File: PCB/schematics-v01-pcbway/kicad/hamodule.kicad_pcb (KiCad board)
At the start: 2 copper layers, 78.4 x 84.3 mm, 10 parts, among them J1 Conn_01x05_Female, J2 Conn_01x05_Female

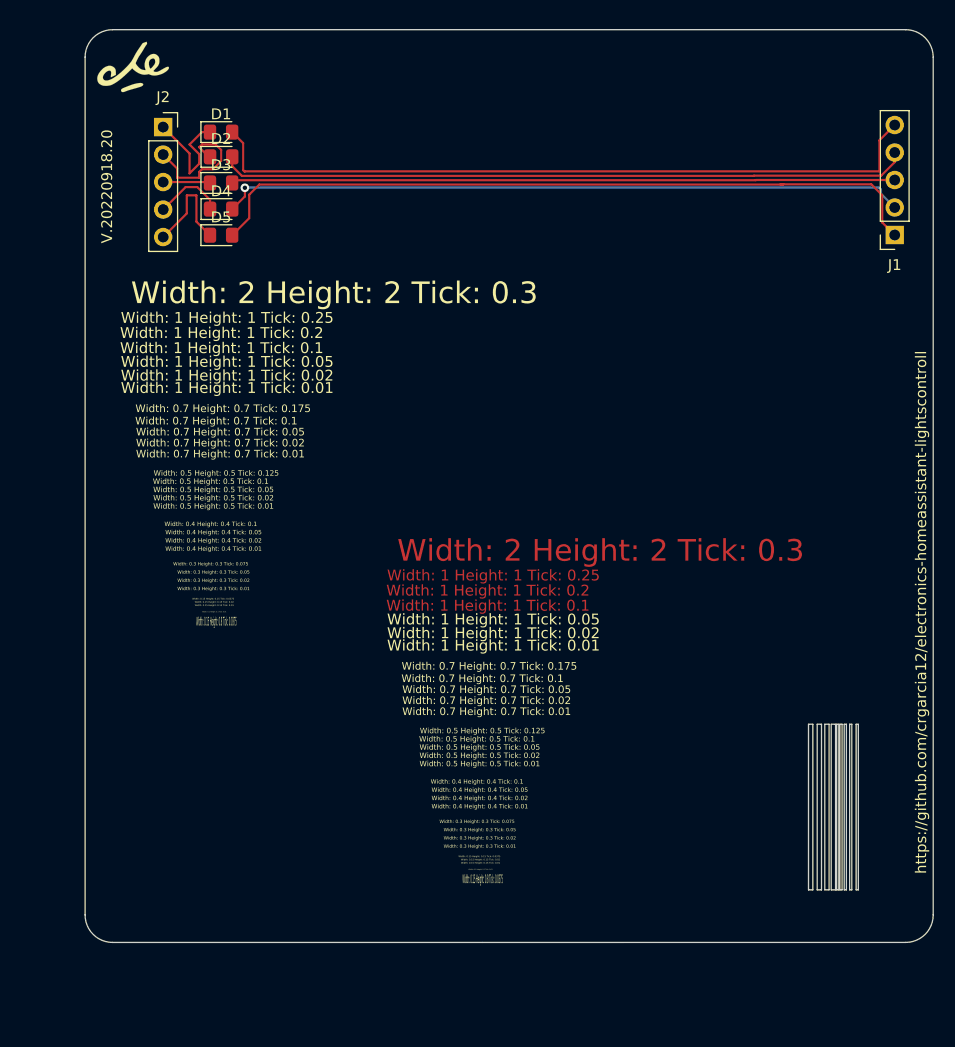
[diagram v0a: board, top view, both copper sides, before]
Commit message: typo in silkscreen
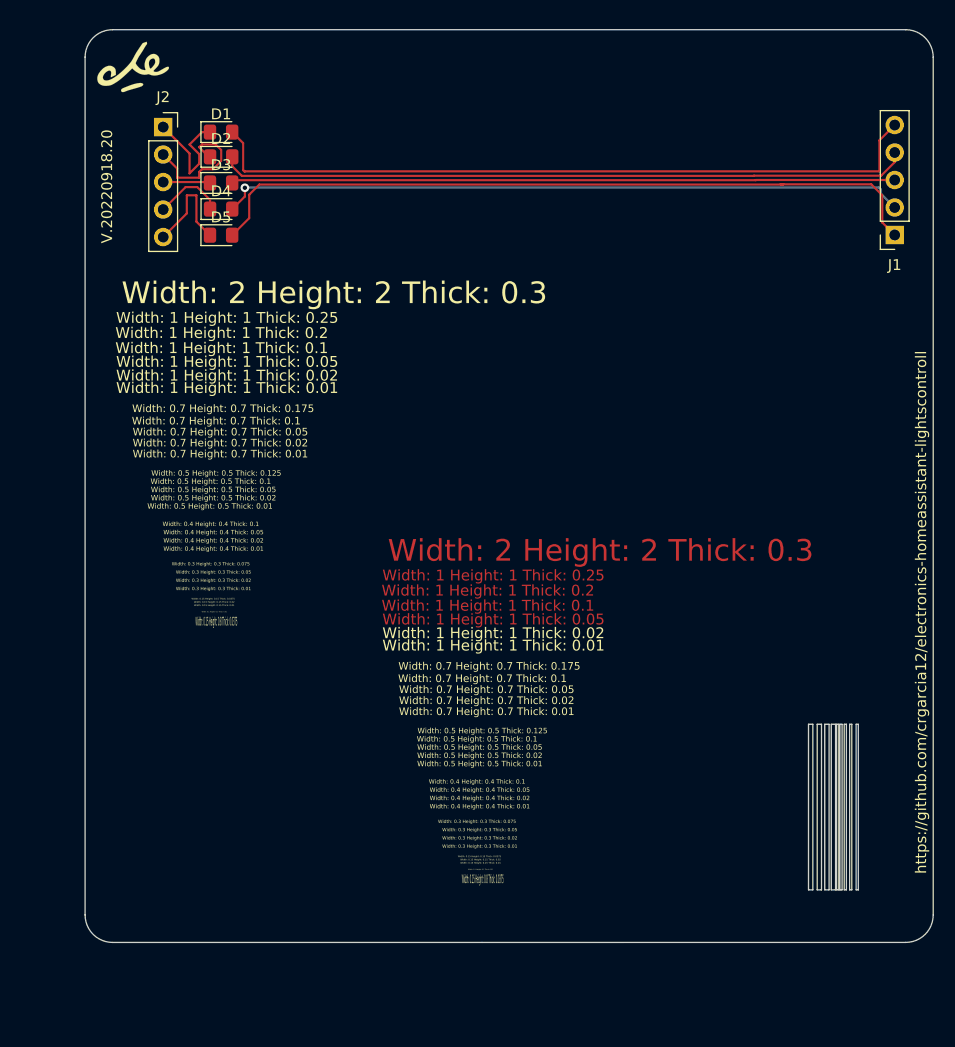
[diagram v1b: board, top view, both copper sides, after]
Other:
- board text added: "Width: 0.1 Height: 0.1 Thick: 0.01"
- board text added: "Width: 0.15 Height: 0.15 Thick: 0.01"
- board text added: "Width: 0.15 Height: 0.15 Thick: 0.02"
- board text added: "Width: 0.15 Height: 0.15 Thick: 0.0375"
- board text added: "Width: 0.15 Height: 0.8 Thick: 0.0375"
- board text added: "Width: 0.3 Height: 0.3 Thick: 0.01"
- board text added: "Width: 0.3 Height: 0.3 Thick: 0.02"
- board text added: "Width: 0.3 Height: 0.3 Thick: 0.05"
- board text added: "Width: 0.3 Height: 0.3 Thick: 0.075"
- board text added: "Width: 0.4 Height: 0.4 Thick: 0.01"
- board text added: "Width: 0.4 Height: 0.4 Thick: 0.02"
- board text added: "Width: 0.4 Height: 0.4 Thick: 0.05"
- board text added: "Width: 0.4 Height: 0.4 Thick: 0.1"
- board text added: "Width: 0.5 Height: 0.5 Thick: 0.01"
- board text added: "Width: 0.5 Height: 0.5 Thick: 0.02"
- board text added: "Width: 0.5 Height: 0.5 Thick: 0.05"
- board text added: "Width: 0.5 Height: 0.5 Thick: 0.1"
- board text added: "Width: 0.5 Height: 0.5 Thick: 0.125"
- board text added: "Width: 0.7 Height: 0.7 Thick: 0.01"
- board text added: "Width: 0.7 Height: 0.7 Thick: 0.02"
- board text added: "Width: 0.7 Height: 0.7 Thick: 0.05"
- board text added: "Width: 0.7 Height: 0.7 Thick: 0.1"
- board text added: "Width: 0.7 Height: 0.7 Thick: 0.175"
- board text added: "Width: 1 Height: 1 Thick: 0.01"
- board text added: "Width: 1 Height: 1 Thick: 0.02"
- board text added: "Width: 1 Height: 1 Thick: 0.05"
- board text added: "Width: 1 Height: 1 Thick: 0.1"
- board text added: "Width: 1 Height: 1 Thick: 0.2"
- board text added: "Width: 1 Height: 1 Thick: 0.25"
- board text added: "Width: 2 Height: 2 Thick: 0.3"
- board text removed: "Width: 0.1 Height: 0.1 Tick: 0.01"
- board text removed: "Width: 0.15 Height: 0.15 Tick: 0.01"
- board text removed: "Width: 0.15 Height: 0.15 Tick: 0.02"
- board text removed: "Width: 0.15 Height: 0.15 Tick: 0.0375"
- board text removed: "Width: 0.15 Height: 0.8 Tick: 0.0375"
- board text removed: "Width: 0.3 Height: 0.3 Tick: 0.01"
- board text removed: "Width: 0.3 Height: 0.3 Tick: 0.02"
- board text removed: "Width: 0.3 Height: 0.3 Tick: 0.05"
- board text removed: "Width: 0.3 Height: 0.3 Tick: 0.075"
- board text removed: "Width: 0.4 Height: 0.4 Tick: 0.01"
- board text removed: "Width: 0.4 Height: 0.4 Tick: 0.02"
- board text removed: "Width: 0.4 Height: 0.4 Tick: 0.05"
- board text removed: "Width: 0.4 Height: 0.4 Tick: 0.1"
- board text removed: "Width: 0.5 Height: 0.5 Tick: 0.01"
- board text removed: "Width: 0.5 Height: 0.5 Tick: 0.02"
- board text removed: "Width: 0.5 Height: 0.5 Tick: 0.05"
- board text removed: "Width: 0.5 Height: 0.5 Tick: 0.1"
- board text removed: "Width: 0.5 Height: 0.5 Tick: 0.125"
- board text removed: "Width: 0.7 Height: 0.7 Tick: 0.01"
- board text removed: "Width: 0.7 Height: 0.7 Tick: 0.02"
- board text removed: "Width: 0.7 Height: 0.7 Tick: 0.05"
- board text removed: "Width: 0.7 Height: 0.7 Tick: 0.1"
- board text removed: "Width: 0.7 Height: 0.7 Tick: 0.175"
- board text removed: "Width: 1 Height: 1 Tick: 0.01"
- board text removed: "Width: 1 Height: 1 Tick: 0.02"
- board text removed: "Width: 1 Height: 1 Tick: 0.05"
- board text removed: "Width: 1 Height: 1 Tick: 0.1"
- board text removed: "Width: 1 Height: 1 Tick: 0.2"
- board text removed: "Width: 1 Height: 1 Tick: 0.25"
- board text removed: "Width: 2 Height: 2 Tick: 0.3"

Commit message: adding components
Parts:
- removed G5: LOGO, icons:depsi
- removed G6: LOGO, icons:flags
- added ?: , , F.Cu at (56.3, 40.2)
- added REF**: Fiducial_0.75mm_Mask1.5mm, Fiducial:Fiducial_0.75mm_Mask1.5mm, F.Cu at (52.6, 92.3)
- added REF**: TestPoint_THTPad_1.0x1.0mm_Drill0.5mm, TestPoint:TestPoint_THTPad_1.0x1.0mm_Drill0.5mm, F.Cu at (89.5, 33.1)
- added REF**: C_1206_3216Metric_Pad1.33x1.80mm_HandSolder, Capacitor_SMD:C_1206_3216Metric_Pad1.33x1.80mm_HandSolder, B.Cu at (97.8, 77.1)
- added REF**: C_0603_1608Metric_Pad1.08x0.95mm_HandSolder, Capacitor_SMD:C_0603_1608Metric_Pad1.08x0.95mm_HandSolder, B.Cu at (58.5, 66.4)
- added REF**: TestPoint_Pad_D2.5mm, TestPoint:TestPoint_Pad_D2.5mm, B.Cu at (81.9, 62.8)
- added REF**: C_1206_3216Metric_Pad1.33x1.80mm_HandSolder, Capacitor_SMD:C_1206_3216Metric_Pad1.33x1.80mm_HandSolder, B.Cu at (58.5, 74.8)
- added REF**: C_0603_1608Metric_Pad1.08x0.95mm_HandSolder, Capacitor_SMD:C_0603_1608Metric_Pad1.08x0.95mm_HandSolder, B.Cu at (89.1, 67.5)
- added REF**: C_0201_0603Metric, Capacitor_SMD:C_0201_0603Metric, B.Cu at (49.5, 60.1)
- added REF**: TestPoint_Pad_D2.5mm, TestPoint:TestPoint_Pad_D2.5mm, B.Cu at (81.9, 71.9)
- added REF**: TestPoint_Pad_D2.5mm, TestPoint:TestPoint_Pad_D2.5mm, B.Cu at (42.3, 56.4)
- added REF**: TestPoint_Pad_D2.5mm, TestPoint:TestPoint_Pad_D2.5mm, B.Cu at (90.6, 56.5)
- added REF**: C_0201_0603Metric, Capacitor_SMD:C_0201_0603Metric, B.Cu at (40.6, 59.6)
- added REF**: Texas_SWRA416_868MHz_915MHz, RF_Antenna:Texas_SWRA416_868MHz_915MHz, F.Cu at (78.4, 91.1)
- added REF**: OSHW-Logo2_14.6x12mm_SilkScreen, Symbol:OSHW-Logo2_14.6x12mm_SilkScreen, B.Cu at (68.0, 54.7)
- added REF**: C_1206_3216Metric_Pad1.33x1.80mm_HandSolder, Capacitor_SMD:C_1206_3216Metric_Pad1.33x1.80mm_HandSolder, B.Cu at (49.7, 76.9)
- added REF**: C_0201_0603Metric, Capacitor_SMD:C_0201_0603Metric, B.Cu at (80.0, 60.2)
- added REF**: TestPoint_Pad_D2.5mm, TestPoint:TestPoint_Pad_D2.5mm, B.Cu at (56.4, 56.5)
- added REF**: C_0201_0603Metric, Capacitor_SMD:C_0201_0603Metric, B.Cu at (97.7, 59.8)
- added REF**: C_0201_0603Metric, Capacitor_SMD:C_0201_0603Metric, B.Cu at (40.6, 59.1)
- added REF**: C_0201_0603Metric, Capacitor_SMD:C_0201_0603Metric, B.Cu at (88.9, 59.2)
- added REF**: TestPoint_Pad_D2.5mm, TestPoint:TestPoint_Pad_D2.5mm, B.Cu at (38.9, 71.8)
- added REF**: C_0603_1608Metric_Pad1.08x0.95mm_HandSolder, Capacitor_SMD:C_0603_1608Metric_Pad1.08x0.95mm_HandSolder, B.Cu at (49.7, 68.5)
- added REF**: C_0603_1608Metric_Pad1.08x0.95mm_HandSolder, Capacitor_SMD:C_0603_1608Metric_Pad1.08x0.95mm_HandSolder, B.Cu at (80.2, 67.5)
- added REF**: Fiducial_1.5mm_Mask4.5mm, Fiducial:Fiducial_1.5mm_Mask4.5mm, F.Cu at (47.1, 103.4)
- added REF**: TestPoint_Pad_D2.5mm, TestPoint:TestPoint_Pad_D2.5mm, B.Cu at (81.7, 56.5)
- added REF**: TestPoint_Pad_D2.5mm, TestPoint:TestPoint_Pad_D2.5mm, B.Cu at (99.6, 62.9)
- added REF**: C_0201_0603Metric, Capacitor_SMD:C_0201_0603Metric, B.Cu at (58.3, 60.2)
- added REF**: C_1206_3216Metric_Pad1.33x1.80mm_HandSolder, Capacitor_SMD:C_1206_3216Metric_Pad1.33x1.80mm_HandSolder, B.Cu at (40.7, 76.9)
- added REF**: C_0603_1608Metric_Pad1.08x0.95mm_HandSolder, Capacitor_SMD:C_0603_1608Metric_Pad1.08x0.95mm_HandSolder, B.Cu at (40.7, 65.1)
- added REF**: TestPoint_Pad_D2.5mm, TestPoint:TestPoint_Pad_D2.5mm, B.Cu at (87.2, 71.9)
- added REF**: C_0603_1608Metric_Pad1.08x0.95mm_HandSolder, Capacitor_SMD:C_0603_1608Metric_Pad1.08x0.95mm_HandSolder, B.Cu at (58.5, 65.2)
- added REF**: TestPoint_Pad_D2.5mm, TestPoint:TestPoint_Pad_D2.5mm, B.Cu at (42.5, 71.8)
- added REF**: TestPoint_Pad_D2.5mm, TestPoint:TestPoint_Pad_D2.5mm, B.Cu at (78.3, 71.9)
- added REF**: C_0603_1608Metric_Pad1.08x0.95mm_HandSolder, Capacitor_SMD:C_0603_1608Metric_Pad1.08x0.95mm_HandSolder, B.Cu at (58.5, 68.6)
- added REF**: TestPoint_Keystone_5000-5004_Miniature, TestPoint:TestPoint_Keystone_5000-5004_Miniature, F.Cu at (85.6, 36.9)
- added REF**: C_0603_1608Metric_Pad1.08x0.95mm_HandSolder, Capacitor_SMD:C_0603_1608Metric_Pad1.08x0.95mm_HandSolder, B.Cu at (58.5, 67.5)
- added REF**: C_0603_1608Metric_Pad1.08x0.95mm_HandSolder, Capacitor_SMD:C_0603_1608Metric_Pad1.08x0.95mm_HandSolder, B.Cu at (89.1, 66.4)
- added REF**: C_0201_0603Metric, Capacitor_SMD:C_0201_0603Metric, B.Cu at (58.3, 58.6)
- added REF**: TestPoint_Pad_D2.5mm, TestPoint:TestPoint_Pad_D2.5mm, B.Cu at (90.8, 71.9)
- added REF**: TestPoint_Pad_D2.5mm, TestPoint:TestPoint_Pad_D2.5mm, B.Cu at (90.8, 62.8)
- added REF**: TestPoint_Pad_D2.5mm, TestPoint:TestPoint_Pad_D2.5mm, B.Cu at (51.5, 71.8)
- added REF**: C_0603_1608Metric_Pad1.08x0.95mm_HandSolder, Capacitor_SMD:C_0603_1608Metric_Pad1.08x0.95mm_HandSolder, B.Cu at (49.7, 67.4)
- added REF**: TestPoint_Pad_D2.5mm, TestPoint:TestPoint_Pad_D2.5mm, B.Cu at (38.7, 56.4)
- added REF**: TestPoint_Pad_D2.5mm, TestPoint:TestPoint_Pad_D2.5mm, B.Cu at (99.6, 72.0)
- added REF**: TestPoint_Pad_D2.5mm, TestPoint:TestPoint_Pad_D2.5mm, B.Cu at (96.0, 62.9)
- added REF**: Fiducial_0.75mm_Mask1.5mm, Fiducial:Fiducial_0.75mm_Mask1.5mm, F.Cu at (96.2, 97.6)
- added REF**: C_0201_0603Metric, Capacitor_SMD:C_0201_0603Metric, B.Cu at (88.9, 58.6)
- added REF**: C_0201_0603Metric, Capacitor_SMD:C_0201_0603Metric, B.Cu at (97.7, 60.3)
- added REF**: TestPoint_Pad_D2.5mm, TestPoint:TestPoint_Pad_D2.5mm, B.Cu at (51.4, 62.7)
- added REF**: TestPoint_Pad_D2.5mm, TestPoint:TestPoint_Pad_D2.5mm, B.Cu at (56.6, 62.8)
- added REF**: C_0201_0603Metric, Capacitor_SMD:C_0201_0603Metric, B.Cu at (49.5, 59.1)
- added REF**: C_0603_1608Metric_Pad1.08x0.95mm_HandSolder, Capacitor_SMD:C_0603_1608Metric_Pad1.08x0.95mm_HandSolder, B.Cu at (80.2, 68.6)
- added REF**: TestPoint_THTPad_1.0x1.0mm_Drill0.5mm, TestPoint:TestPoint_THTPad_1.0x1.0mm_Drill0.5mm, F.Cu at (84.1, 33.2)
- added REF**: Texas_SWRA117D_2.4GHz_Right, RF_Antenna:Texas_SWRA117D_2.4GHz_Right, F.Cu at (54.7, 90.2)
- added REF**: Fiducial_0.5mm_Mask1mm, Fiducial:Fiducial_0.5mm_Mask1mm, F.Cu at (33.7, 91.3)
- added REF**: TestPoint_Pad_D2.5mm, TestPoint:TestPoint_Pad_D2.5mm, F.Cu at (95.1, 36.9)
- added REF**: Fiducial_0.5mm_Mask1.5mm, Fiducial:Fiducial_0.5mm_Mask1.5mm, F.Cu at (47.0, 95.8)
- added REF**: TestPoint_THTPad_1.0x1.0mm_Drill0.5mm, TestPoint:TestPoint_THTPad_1.0x1.0mm_Drill0.5mm, F.Cu at (78.5, 33.2)
- added REF**: Fiducial_0.5mm_Mask1.5mm, Fiducial:Fiducial_0.5mm_Mask1.5mm, F.Cu at (47.0, 91.6)
- added REF**: Fiducial_0.75mm_Mask2.25mm, Fiducial:Fiducial_0.75mm_Mask2.25mm, F.Cu at (47.1, 99.0)
- added REF**: TestPoint_Bridge_Pitch2.0mm_Drill0.7mm, TestPoint:TestPoint_Bridge_Pitch2.0mm_Drill0.7mm, F.Cu at (78.7, 35.8)
- added REF**: Fiducial_0.5mm_Mask1.5mm, Fiducial:Fiducial_0.5mm_Mask1.5mm, F.Cu at (101.2, 90.2)
- added REF**: Fiducial_1.5mm_Mask3mm, Fiducial:Fiducial_1.5mm_Mask3mm, F.Cu at (96.2, 102.1)
- added REF**: MountingHole_2.2mm_M2_Pad_TopOnly, MountingHole:MountingHole_2.2mm_M2_Pad_TopOnly, F.Cu at (60.7, 34.7)
- added REF**: Fiducial_0.5mm_Mask1.5mm, Fiducial:Fiducial_0.5mm_Mask1.5mm, F.Cu at (101.2, 94.4)
- added REF**: TestPoint_Keystone_5010-5014_Multipurpose, TestPoint:TestPoint_Keystone_5010-5014_Multipurpose, F.Cu at (89.8, 37.0)
- added REF**: Fiducial_1.5mm_Mask3mm, Fiducial:Fiducial_1.5mm_Mask3mm, F.Cu at (33.9, 103.3)
- added REF**: MountingHole_2.2mm_M2_Pad_Via, MountingHole:MountingHole_2.2mm_M2_Pad_Via, F.Cu at (50.8, 40.0)
- added REF**: TestPoint_Pad_2.0x2.0mm, TestPoint:TestPoint_Pad_2.0x2.0mm, F.Cu at (95.2, 41.1)
- added REF**: MountingHole_2.1mm, MountingHole:MountingHole_2.1mm, F.Cu at (50.7, 34.4)
- added REF**: Fiducial_0.5mm_Mask1mm, Fiducial:Fiducial_0.5mm_Mask1mm, F.Cu at (33.7, 95.5)
- added REF**: Fiducial_0.75mm_Mask2.25mm, Fiducial:Fiducial_0.75mm_Mask2.25mm, F.Cu at (101.3, 97.6)
- added REF**: Fiducial_0.5mm_Mask1mm, Fiducial:Fiducial_0.5mm_Mask1mm, F.Cu at (96.0, 94.3)
- added REF**: Fiducial_0.75mm_Mask1.5mm, Fiducial:Fiducial_0.75mm_Mask1.5mm, F.Cu at (33.8, 98.8)
- added REF**: C_1206_3216Metric_Pad1.33x1.80mm_HandSolder, Capacitor_SMD:C_1206_3216Metric_Pad1.33x1.80mm_HandSolder, B.Cu at (89.0, 79.1)
- added REF**: C_0603_1608Metric_Pad1.08x0.95mm_HandSolder, Capacitor_SMD:C_0603_1608Metric_Pad1.08x0.95mm_HandSolder, B.Cu at (97.9, 68.7)
- added REF**: TestPoint_Pad_D2.5mm, TestPoint:TestPoint_Pad_D2.5mm, B.Cu at (60.2, 62.8)
- added REF**: OSHW-Logo2_7.3x6mm_SilkScreen, Symbol:OSHW-Logo2_7.3x6mm_SilkScreen, B.Cu at (68.0, 37.8)
- added REF**: C_0201_0603Metric, Capacitor_SMD:C_0201_0603Metric, B.Cu at (49.5, 59.6)
- added REF**: MountingHole_2.2mm_M2_ISO7380_Pad_TopBottom, MountingHole:MountingHole_2.2mm_M2_ISO7380_Pad_TopBottom, F.Cu at (55.6, 34.6)
- added REF**: C_1206_3216Metric_Pad1.33x1.80mm_HandSolder, Capacitor_SMD:C_1206_3216Metric_Pad1.33x1.80mm_HandSolder, B.Cu at (97.8, 81.3)
- added REF**: TestPoint_Pad_D2.5mm, TestPoint:TestPoint_Pad_D2.5mm, B.Cu at (51.2, 56.4)
- added REF**: C_0603_1608Metric_Pad1.08x0.95mm_HandSolder, Capacitor_SMD:C_0603_1608Metric_Pad1.08x0.95mm_HandSolder, B.Cu at (40.8, 66.3)
- added REF**: C_0603_1608Metric_Pad1.08x0.95mm_HandSolder, Capacitor_SMD:C_0603_1608Metric_Pad1.08x0.95mm_HandSolder, B.Cu at (97.9, 67.6)
- added REF**: TestPoint_Pad_D2.5mm, TestPoint:TestPoint_Pad_D2.5mm, B.Cu at (56.7, 71.9)
- added REF**: C_1206_3216Metric_Pad1.33x1.80mm_HandSolder, Capacitor_SMD:C_1206_3216Metric_Pad1.33x1.80mm_HandSolder, B.Cu at (80.1, 79.1)
- added REF**: TestPoint_Pad_D2.5mm, TestPoint:TestPoint_Pad_D2.5mm, B.Cu at (78.1, 56.5)
- added REF**: C_0201_0603Metric, Capacitor_SMD:C_0201_0603Metric, B.Cu at (88.9, 59.7)
- added REF**: TestPoint_Pad_D2.5mm, TestPoint:TestPoint_Pad_D2.5mm, B.Cu at (60.0, 56.5)
- added REF**: C_0201_0603Metric, Capacitor_SMD:C_0201_0603Metric, B.Cu at (88.9, 60.2)
- added REF**: Fiducial_0.75mm_Mask1.5mm, Fiducial:Fiducial_0.75mm_Mask1.5mm, F.Cu at (55.3, 92.3)
- added REF**: C_0201_0603Metric, Capacitor_SMD:C_0201_0603Metric, B.Cu at (40.6, 60.1)
- added REF**: C_0603_1608Metric_Pad1.08x0.95mm_HandSolder, Capacitor_SMD:C_0603_1608Metric_Pad1.08x0.95mm_HandSolder, B.Cu at (80.1, 65.2)
- added REF**: C_1206_3216Metric_Pad1.33x1.80mm_HandSolder, Capacitor_SMD:C_1206_3216Metric_Pad1.33x1.80mm_HandSolder, B.Cu at (80.1, 77.0)
- added REF**: TestPoint_Pad_D2.5mm, TestPoint:TestPoint_Pad_D2.5mm, B.Cu at (87.2, 62.8)
- added REF**: C_1206_3216Metric_Pad1.33x1.80mm_HandSolder, Capacitor_SMD:C_1206_3216Metric_Pad1.33x1.80mm_HandSolder, B.Cu at (89.0, 77.0)
- added REF**: C_1206_3216Metric_Pad1.33x1.80mm_HandSolder, Capacitor_SMD:C_1206_3216Metric_Pad1.33x1.80mm_HandSolder, B.Cu at (89.0, 81.2)
- added REF**: C_0603_1608Metric_Pad1.08x0.95mm_HandSolder, Capacitor_SMD:C_0603_1608Metric_Pad1.08x0.95mm_HandSolder, B.Cu at (97.9, 66.5)
- added REF**: C_0603_1608Metric_Pad1.08x0.95mm_HandSolder, Capacitor_SMD:C_0603_1608Metric_Pad1.08x0.95mm_HandSolder, B.Cu at (49.7, 65.1)
- added REF**: C_1206_3216Metric_Pad1.33x1.80mm_HandSolder, Capacitor_SMD:C_1206_3216Metric_Pad1.33x1.80mm_HandSolder, B.Cu at (40.7, 81.1)
- added REF**: C_0603_1608Metric_Pad1.08x0.95mm_HandSolder, Capacitor_SMD:C_0603_1608Metric_Pad1.08x0.95mm_HandSolder, B.Cu at (49.7, 66.3)
- added REF**: Fiducial_1.5mm_Mask4.5mm, Fiducial:Fiducial_1.5mm_Mask4.5mm, F.Cu at (101.3, 102.0)
- added REF**: TestPoint_Pad_D2.5mm, TestPoint:TestPoint_Pad_D2.5mm, B.Cu at (38.9, 62.7)
- added REF**: C_0201_0603Metric, Capacitor_SMD:C_0201_0603Metric, B.Cu at (58.3, 59.7)
- added REF**: C_1206_3216Metric_Pad1.33x1.80mm_HandSolder, Capacitor_SMD:C_1206_3216Metric_Pad1.33x1.80mm_HandSolder, B.Cu at (58.5, 81.2)
- added REF**: C_1206_3216Metric_Pad1.33x1.80mm_HandSolder, Capacitor_SMD:C_1206_3216Metric_Pad1.33x1.80mm_HandSolder, B.Cu at (58.5, 77.0)
- added REF**: TestPoint_Pad_D2.5mm, TestPoint:TestPoint_Pad_D2.5mm, B.Cu at (99.4, 56.6)
- added REF**: C_0201_0603Metric, Capacitor_SMD:C_0201_0603Metric, B.Cu at (40.6, 58.5)
- added REF**: C_0603_1608Metric_Pad1.08x0.95mm_HandSolder, Capacitor_SMD:C_0603_1608Metric_Pad1.08x0.95mm_HandSolder, B.Cu at (97.8, 65.3)
- added REF**: C_0201_0603Metric, Capacitor_SMD:C_0201_0603Metric, B.Cu at (97.7, 59.3)
- added REF**: C_1206_3216Metric_Pad1.33x1.80mm_HandSolder, Capacitor_SMD:C_1206_3216Metric_Pad1.33x1.80mm_HandSolder, B.Cu at (58.5, 79.1)
- added REF**: C_0201_0603Metric, Capacitor_SMD:C_0201_0603Metric, B.Cu at (97.7, 58.7)
- added REF**: Fiducial_0.5mm_Mask1mm, Fiducial:Fiducial_0.5mm_Mask1mm, F.Cu at (96.0, 90.1)
- added REF**: C_0201_0603Metric, Capacitor_SMD:C_0201_0603Metric, B.Cu at (49.5, 58.5)
- added REF**: C_0603_1608Metric_Pad1.08x0.95mm_HandSolder, Capacitor_SMD:C_0603_1608Metric_Pad1.08x0.95mm_HandSolder, B.Cu at (40.8, 68.5)
- added REF**: C_1206_3216Metric_Pad1.33x1.80mm_HandSolder, Capacitor_SMD:C_1206_3216Metric_Pad1.33x1.80mm_HandSolder, B.Cu at (80.1, 74.8)
- added REF**: TestPoint_Pad_D2.5mm, TestPoint:TestPoint_Pad_D2.5mm, B.Cu at (96.0, 72.0)
- added REF**: C_1206_3216Metric_Pad1.33x1.80mm_HandSolder, Capacitor_SMD:C_1206_3216Metric_Pad1.33x1.80mm_HandSolder, B.Cu at (49.7, 81.1)
- added REF**: C_0603_1608Metric_Pad1.08x0.95mm_HandSolder, Capacitor_SMD:C_0603_1608Metric_Pad1.08x0.95mm_HandSolder, B.Cu at (89.1, 68.6)
- added REF**: C_1206_3216Metric_Pad1.33x1.80mm_HandSolder, Capacitor_SMD:C_1206_3216Metric_Pad1.33x1.80mm_HandSolder, B.Cu at (89.0, 74.8)
- added REF**: C_1206_3216Metric_Pad1.33x1.80mm_HandSolder, Capacitor_SMD:C_1206_3216Metric_Pad1.33x1.80mm_HandSolder, B.Cu at (49.7, 79.0)
- added REF**: C_0201_0603Metric, Capacitor_SMD:C_0201_0603Metric, B.Cu at (58.3, 59.2)
- added REF**: C_0201_0603Metric, Capacitor_SMD:C_0201_0603Metric, B.Cu at (80.0, 59.2)
- added REF**: Fiducial_0.75mm_Mask1.5mm, Fiducial:Fiducial_0.75mm_Mask1.5mm, F.Cu at (69.4, 99.0)
- added REF**: TestPoint_Pad_D2.5mm, TestPoint:TestPoint_Pad_D2.5mm, B.Cu at (60.3, 71.9)
- added REF**: TestPoint_Pad_D2.5mm, TestPoint:TestPoint_Pad_D2.5mm, B.Cu at (87.0, 56.5)
- added REF**: C_1206_3216Metric_Pad1.33x1.80mm_HandSolder, Capacitor_SMD:C_1206_3216Metric_Pad1.33x1.80mm_HandSolder, B.Cu at (97.8, 74.9)
- added REF**: TestPoint_Pad_D2.5mm, TestPoint:TestPoint_Pad_D2.5mm, B.Cu at (42.5, 62.7)
- added REF**: C_1206_3216Metric_Pad1.33x1.80mm_HandSolder, Capacitor_SMD:C_1206_3216Metric_Pad1.33x1.80mm_HandSolder, B.Cu at (40.7, 79.0)
- added REF**: C_0603_1608Metric_Pad1.08x0.95mm_HandSolder, Capacitor_SMD:C_0603_1608Metric_Pad1.08x0.95mm_HandSolder, B.Cu at (80.2, 66.4)
- added REF**: C_1206_3216Metric_Pad1.33x1.80mm_HandSolder, Capacitor_SMD:C_1206_3216Metric_Pad1.33x1.80mm_HandSolder, B.Cu at (97.8, 79.2)
- added REF**: C_1206_3216Metric_Pad1.33x1.80mm_HandSolder, Capacitor_SMD:C_1206_3216Metric_Pad1.33x1.80mm_HandSolder, B.Cu at (40.7, 74.7)
- added REF**: TestPoint_Pad_D2.5mm, TestPoint:TestPoint_Pad_D2.5mm, B.Cu at (95.8, 56.6)
- added REF**: OSHW-Logo2_9.8x8mm_SilkScreen, Symbol:OSHW-Logo2_9.8x8mm_SilkScreen, B.Cu at (67.9, 45.2)
- added REF**: DINRailAdapter_3xM3_PhoenixContact_1201578, MountingEquipment:DINRailAdapter_3xM3_PhoenixContact_1201578, F.Cu at (72.2, 105.4)
- added REF**: TestPoint_Pad_D2.5mm, TestPoint:TestPoint_Pad_D2.5mm, B.Cu at (78.3, 62.8)
- added REF**: TestPoint_Pad_D2.5mm, TestPoint:TestPoint_Pad_D2.5mm, B.Cu at (47.9, 71.8)
- added REF**: TestPoint_Pad_D2.5mm, TestPoint:TestPoint_Pad_D2.5mm, B.Cu at (47.8, 62.7)
- added REF**: C_0603_1608Metric_Pad1.08x0.95mm_HandSolder, Capacitor_SMD:C_0603_1608Metric_Pad1.08x0.95mm_HandSolder, B.Cu at (89.0, 65.2)
- added REF**: C_0201_0603Metric, Capacitor_SMD:C_0201_0603Metric, B.Cu at (80.0, 58.6)
- added REF**: C_0201_0603Metric, Capacitor_SMD:C_0201_0603Metric, B.Cu at (80.0, 59.7)
- added REF**: C_1206_3216Metric_Pad1.33x1.80mm_HandSolder, Capacitor_SMD:C_1206_3216Metric_Pad1.33x1.80mm_HandSolder, B.Cu at (80.1, 81.2)
- added REF**: C_0603_1608Metric_Pad1.08x0.95mm_HandSolder, Capacitor_SMD:C_0603_1608Metric_Pad1.08x0.95mm_HandSolder, B.Cu at (40.8, 67.4)
- added REF**: TestPoint_Pad_D2.5mm, TestPoint:TestPoint_Pad_D2.5mm, B.Cu at (47.6, 56.4)
- added REF**: C_1206_3216Metric_Pad1.33x1.80mm_HandSolder, Capacitor_SMD:C_1206_3216Metric_Pad1.33x1.80mm_HandSolder, B.Cu at (49.7, 74.7)
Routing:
- net (no net): track 0.00 -> 386.0 mm
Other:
- board size 78.4 x 84.3 mm -> 78 x 82.1 mm
- board text added: "REF**"

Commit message: [V01] github workflow
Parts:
- added ?: , , F.Cu at (104.3, 33.9)
- added ?: , , F.Cu at (61.9, 93.1)
- added REF**: TestPoint_THTPad_2.5x2.5mm_Drill1.2mm, TestPoint:TestPoint_THTPad_2.5x2.5mm_Drill1.2mm, F.Cu at (33.7, 34.3)
- moved G1 4.28 mm to (39.5, 33.8)
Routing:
- net (no net): track 386.0 -> 1371.0 mm
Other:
- outline, holes or cut-outs redrawn
- board text added: "V.20220927.01"
- board text added: "https://github.com/crgarcia12/electronics-tester-pcb"
- board text removed: "V.20220918.20"
